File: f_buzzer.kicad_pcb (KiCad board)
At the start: 2 copper layers, 71.5 x 44 mm, 11 parts, among them U1 SN74123N

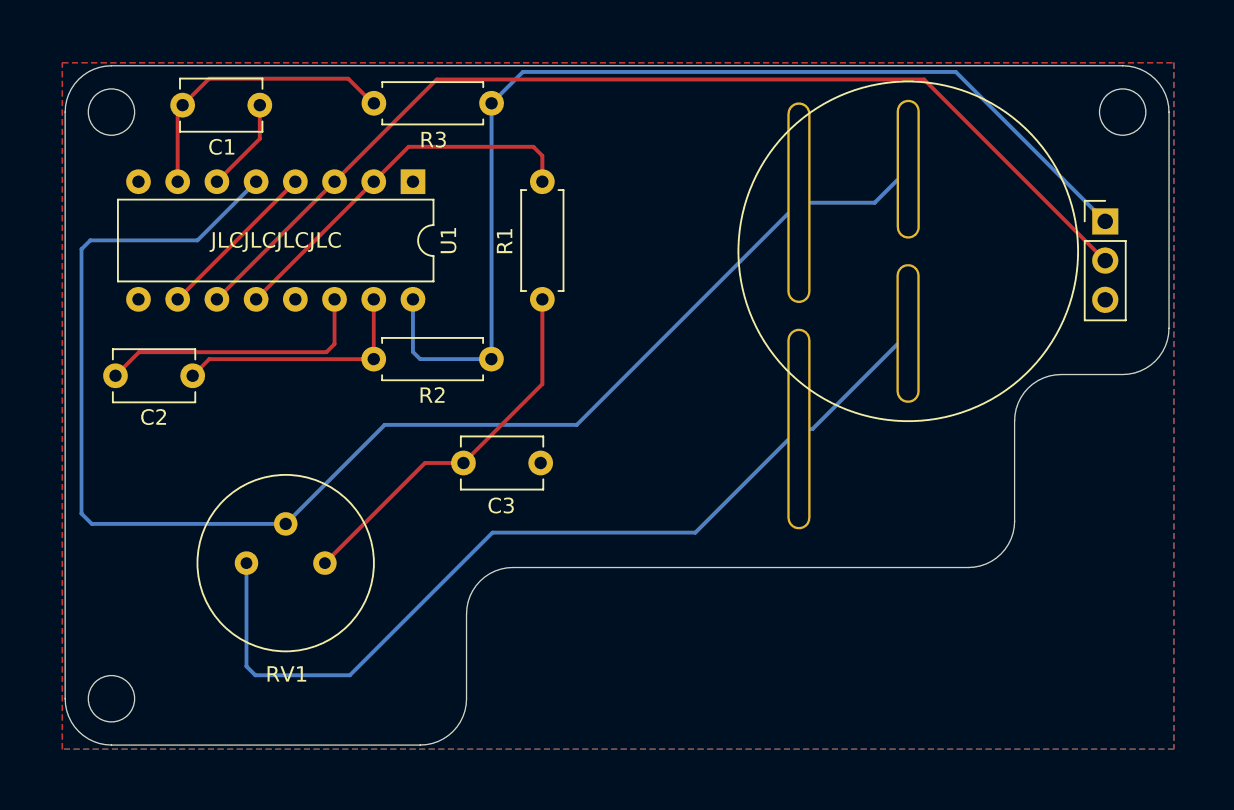
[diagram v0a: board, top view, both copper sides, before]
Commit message: Changed the potentiometer footprint
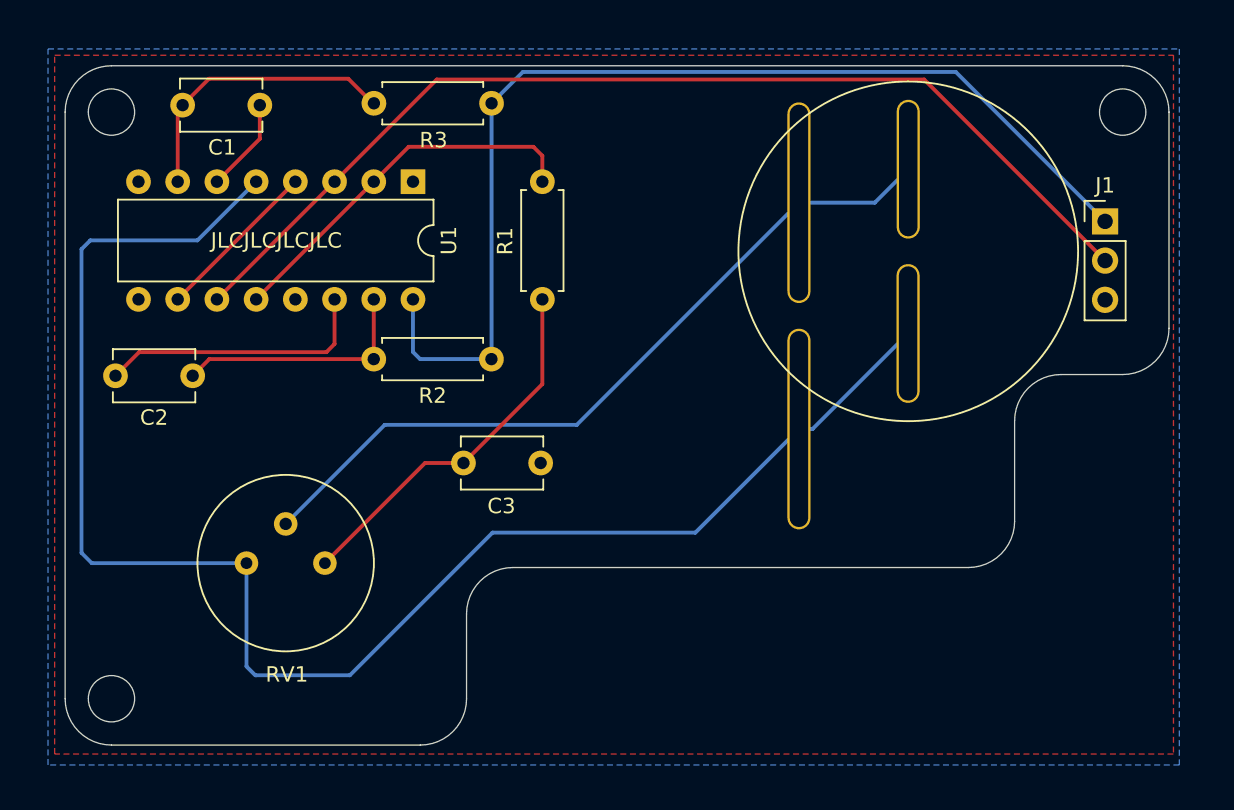
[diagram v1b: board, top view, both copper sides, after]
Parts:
- removed REF**: PinHeader_1x03_P2.54mm_Horizontal, f_buzzer:PinHeader_1x03_P2.54mm_Horizontal
- added J1: Conn_01x03, f_buzzer:PinHeader_1x03_P2.54mm_Horizontal, F.Cu at (181.6, 86.2)
- C3: value C -> 7n
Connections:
- net /DVR renamed DVR
- BZ2 pad 2: Net-(BZ1-Pad2) -> Net-(BZ2-Pad2)
- RV1 pad 1: Net-(BZ1-Pad1) -> Net-(C3-Pad1)
- RV1 pad 2: Net-(BZ1-Pad2) -> Net-(BZ1-Pad1)
- RV1 pad 3: Net-(C3-Pad1) -> Net-(BZ1-Pad2)
- U1 pad 16: VCC -> Net-(U1-Pad16)
- U1 pad 5: Net-(BZ1-Pad1) -> Net-(BZ1-Pad2)
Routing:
- net Net-(BZ1-Pad1): track 93.6 -> 49.8 mm
- net Net-(BZ1-Pad2): track 59.0 -> 102.7 mm

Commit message: Update to KiCad 6
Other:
- net class Default removed

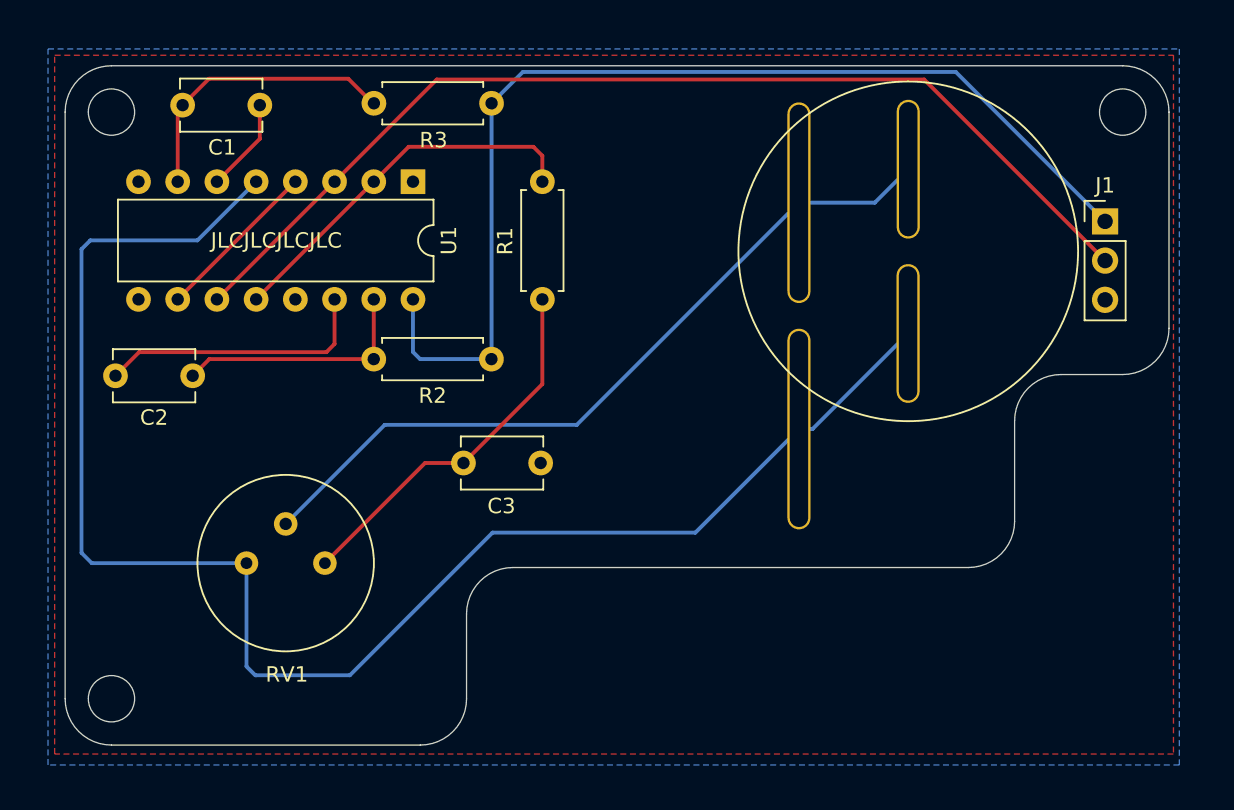
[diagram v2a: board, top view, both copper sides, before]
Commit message: Rearranged the components
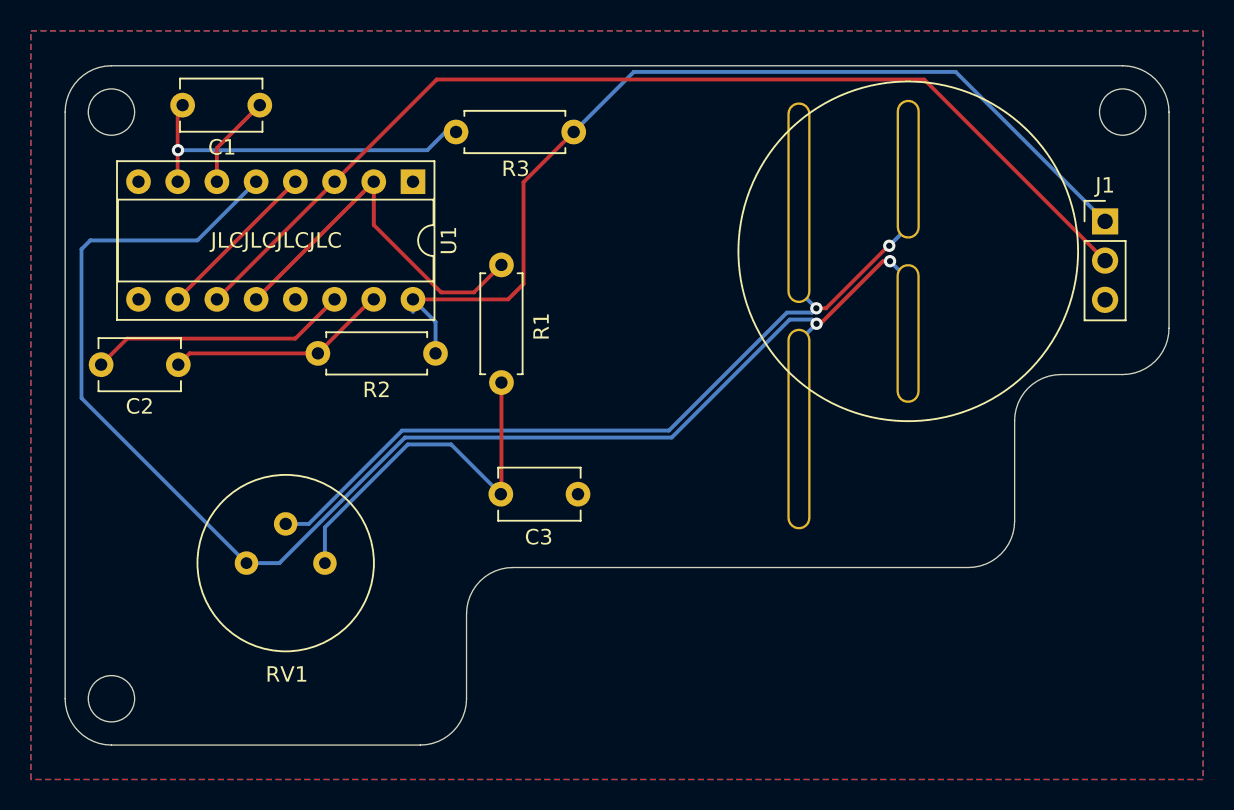
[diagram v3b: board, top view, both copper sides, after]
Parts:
- U1: footprint Package_DIP:DIP-16_W7.62mm -> Package_DIP:DIP-16_W7.62mm_Socket
- moved R1 6.01 mm to (142.5, 89.0)
- moved R3 5.64 mm to (139.5, 80.4)
- moved R2 3.64 mm to (138.2, 94.8)
- moved C3 3.15 mm to (142.4, 103.9)
- moved C2 1.18 mm to (116.5, 95.5)
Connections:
- BZ2 pad 2: Net-(BZ2-Pad2) -> Net-(BZ1-Pad2)
- U1 pad 13: Net-(U1-Pad13) -> unconnected-(U1-Pad13)
- U1 pad 16: Net-(U1-Pad16) -> VCC
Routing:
- net Net-(BZ1-Pad1): track 49.8 -> 59.3 mm, vias 0 -> 2
- net VCC: track 69.9 -> 63.7 mm
- net Net-(C1-Pad2): track 18.8 -> 23.6 mm, vias 0 -> 1
- net Net-(BZ1-Pad2): track 102.7 -> 100.3 mm, vias 0 -> 2
- net Net-(C2-Pad2): track 16.1 -> 14.4 mm
- net Net-(C2-Pad1): track 17.9 -> 16.9 mm
